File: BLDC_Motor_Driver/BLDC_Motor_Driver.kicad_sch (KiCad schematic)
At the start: 21 parts, among them J1 Conn_01x03_Socket, J2 Conn_01x05_Socket, U1 TMC9660ATB+T, U101 TMC9660, U102 SN74LVC3G17

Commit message: finished power circuitry
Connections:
- net +5V renamed 5V_DRV
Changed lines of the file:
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@@
 	(wire
 		(pts
-			(xy 19.05 111.76) (xy 19.05 114.3)
-		)
-		(stroke
-			(width 0)
-			(type default)
-		)
-	)
-	(wire
-		(pts
 			(xy 34.29 124.46) (xy 36.83 124.46)
 		)
@@
 	(wire
 		(pts
-			(xy 19.05 114.3) (xy 36.83 114.3)
+			(xy 20.32 114.3) (xy 36.83 114.3)
 		)
 		(stroke
@@
 		)
 	)
+	(label "5V_DRV"
+		(at 248.92 121.92 0)
+		(effects
+			(font
+				(size 1.27 1.27)
+			)
+			(justify left bottom)
+		)
+	)
 	(label "DRIVER_CPO"
 		(at -172.72 173.99 0)
@@
 		)
 	)
+	(label "5V_DRV"
+		(at 195.58 107.95 180)
+		(effects
+			(font
+				(size 1.27 1.27)
+			)
+			(justify right bottom)
+		)
+	)
 	(label "HS_Y"
 		(at 175.26 58.42 180)
@@
 		)
 	)
+	(label "5V_DRV"
+		(at 20.32 114.3 180)
+		(effects
+			(font
+				(size 1.27 1.27)
+			)
+			(justify right bottom)
+		)
+	)
 	(label "CSP_V"
 		(at 194.31 39.37 0)
@@
 	)
 	(symbol
-		(lib_id "power:+5V")
-		(at 19.05 111.76 0)
-		(unit 1)
-		(exclude_from_sim no)
-		(in_bom yes)
-		(on_board yes)
-		(dnp no)
-		(property "Reference" "#PWR0120"
-			(at 19.05 115.57 0)
-			(effects
-				(font
-					(size 1.27 1.27)
-				)
-				(hide yes)
-			)
-		)
-		(property "Value" "+5V"
-			(at 19.05 107.95 0)
-			(effects
-				(font
-					(size 1.27 1.27)
-				)
-			)
-		)
-		(property "Footprint" ""
-			(at 19.05 111.76 0)
-			(effects
-				(font
-					(size 1.27 1.27)
-				)
-				(hide yes)
-			)
-		)
-		(property "Datasheet" ""
-			(at 19.05 111.76 0)
-			(effects
-				(font
-					(size 1.27 1.27)
-				)
-				(hide yes)
-			)
-		)
-		(property "Description" "Power symbol creates a global label with name \"+5V\""
-			(at 19.05 111.76 0)
-			(effects
-				(font
-					(size 1.27 1.27)
-				)
-				(hide yes)
-			)
-		)
-		(pin "1"
-		)
-		(instances
-			(project ""
-				(path "/f8816ca8-d12a-4d6e-83e4-586d8ea9408b"
-					(reference "#PWR0120")
-					(unit 1)
-				)
-			)
-		)
-	)
-	(symbol
 		(lib_id "power:GND")
 		(at 46.99 58.42 0)
@@
 	)
 	(symbol
-		(lib_id "power:+5V")
-		(at 195.58 107.95 0)
-		(unit 1)
-		(exclude_from_sim no)
-		(in_bom yes)
-		(on_board yes)
-		(dnp no)
-		(property "Reference" "#PWR0126"
-			(at 195.58 111.76 0)
-			(effects
-				(font
-					(size 1.27 1.27)
-				)
-				(hide yes)
-			)
-		)
-		(property "Value" "+5V"
-			(at 195.58 104.14 0)
-			(effects
-				(font
-					(size 1.27 1.27)
-				)
-			)
-		)
-		(property "Footprint" ""
-			(at 195.58 107.95 0)
-			(effects
-				(font
-					(size 1.27 1.27)
-				)
-				(hide yes)
-			)
-		)
-		(property "Datasheet" ""
-			(at 195.58 107.95 0)
-			(effects
-				(font
-					(size 1.27 1.27)
-				)
-				(hide yes)
-			)
-		)
-		(property "Description" "Power symbol creates a global label with name \"+5V\""
-			(at 195.58 107.95 0)
-			(effects
-				(font
-					(size 1.27 1.27)
-				)
-				(hide yes)
-			)
-		)
-		(pin "1"
-		)
-		(instances
-			(project "BLDC_Motor_Driver"
-				(path "/f8816ca8-d12a-4d6e-83e4-586d8ea9408b"
-					(reference "#PWR0126")
-					(unit 1)
-				)
-			)
-		)
-	)
-	(symbol
 		(lib_id "Device:C")
 		(at 69.85 35.56 0)
@@
 					(unit 1)
 				)
-			)
-		)
-	)
-	(symbol
-		(lib_id "power:+5V")
-		(at 248.92 121.92 0)
-		(unit 1)
-		(exclude_from_sim no)
-		(in_bom yes)
-		(on_board yes)
-		(dnp no)
-		(property "Reference" "#PWR0121"
-			(at 248.92 125.73 0)
-			(effects
-				(font
-					(size 1.27 1.27)
-				)
-				(hide yes)
-			)
-		)
-		(property "Value" "+5V"
-			(at 248.92 118.11 0)
-			(effects
-				(font
-					(size 1.27 1.27)
-				)
-			)
-		)
-		(property "Footprint" ""
-			(at 248.92 121.92 0)
-			(effects
-				(font
-					(size 1.27 1.27)
-				)
-				(hide yes)
-			)
-		)
-		(property "Datasheet" ""
-			(at 248.92 121.92 0)
-			(effects
-				(font
-					(size 1.27 1.27)
-				)
-				(hide yes)
-			)
-		)
-		(property "Description" "Power symbol creates a global label with name \"+5V\""
-			(at 248.92 121.92 0)
-			(effects
-				(font
-					(size 1.27 1.27)
-				)
-				(hide yes)
-			)
-		)
-		(pin "1"
-		)
-		(instances
-			(project "BLDC_Motor_Driver"
-				(path "/f8816ca8-d12a-4d6e-83e4-586d8ea9408b"
-					(reference "#PWR0121")
-					(unit 1)
-				)

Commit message: hall effect done, adding testpoints/connectors
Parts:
- removed U1: TMC9660ATB+T, 21-100060_T6499+2C_ADI, symbol TMC9660ATB:TMC9660ATB+T
- added C112, C114, C115: 1nF, Capacitor_SMD:C_0603_1608Metric, symbol Device:C
- added R111, R112, R113: 4.7k, Resistor_SMD:R_0603_1608Metric, symbol Device:R_US
- added TP101, TP102, TP103, TP104, TP105, TP106, TP107: TestPoint, symbol Connector:TestPoint
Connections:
- net +1V8: now also TP101.1
- net 5V_DRV: now also R111.1, R112.1, R113.1, TP106.1
- net DRIVER_DRV_EN: now also TP104.1
- net DRIVER_FAULTN: now also TP103.1
- net DRIVER_RSTN: now also TP105.1
- net DRIVER_V_{BUCK}: now also TP102.1
- net DRIVER_V_{EXT2}: now also TP107.1
- net GND: now also C112.2, C114.2, C115.2
- net HALL_U_CONN: now also R101.1
- net HALL_V_CONN: now also R102.1
- net HALL_W_CONN: now also R106.1
- net at R102.2: now also U102.3 (2A), C114.1, R112.2
- net at R106.2: now also U102.6 (3A), C112.1, R111.2
- net at R101.2: now also U102.1 (1A), C115.1, R113.2
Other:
- note added: "Testpoints"

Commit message: new GateDriver subsheet. reorg connectors to root sheet
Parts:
- removed C107: 1uF, Capacitor_SMD:C_1206_3216Metric, symbol Device:C
- removed C109: 100nF, Capacitor_SMD:C_0805_2012Metric, symbol Device:C
- removed C110: 100nF, Capacitor_SMD:C_0603_1608Metric, symbol Device:C
- removed C112, C114, C115: 1nF, Capacitor_SMD:C_0603_1608Metric, symbol Device:C
- removed C3: 10uF, Capacitor_SMD:C_0603_1608Metric, symbol Device:C
- removed C4, C5: 10uF, Capacitor_SMD:C_0805_2012Metric, symbol Device:C
- removed C6: 1uF, Capacitor_SMD:C_0603_1608Metric, symbol Device:C
- removed C7: C, symbol Device:C
- removed C8: 10uF, symbol Device:C
- removed L1: 27uH, Inductor_SMD:L_APV_ANR6045, symbol Device:L
- removed R101, R102, R106, R111, R112, R113: 4.7k, Resistor_SMD:R_0603_1608Metric, symbol Device:R_US
- removed U101: TMC9660, Package_QFN:QFN-64-1EP_9x9mm_P0.5mm_EP6.3x6.3mm, symbol Driver_Motor_Analog:TMC9660
- removed U102: SN74LVC3G17, Package_SO:VSSOP-8_2.3x2mm_P0.5mm, symbol Buffer_Texas:SN74LVC3G17
- added D1: RED LED, LED_SMD:LED_0603_1608Metric, symbol Device:LED
- added D2: ORANGE LED, LED_SMD:LED_0603_1608Metric, symbol Device:LED
- added D3: GREEN LED, LED_SMD:LED_0603_1608Metric, symbol Device:LED
- added D4: BLUE LED, LED_SMD:LED_0603_1608Metric, symbol Device:LED
- added J3: Conn_01x02, TerminalBlock_Phoenix:TerminalBlock_Phoenix_MKDS-1-2-3.81_1x02_P3.81mm_Horizontal, symbol Connector_Generic:Conn_01x02
- added J4: USB4105-GF-A, Connector_USB:USB_C_Receptacle_GCT_USB4105-xx-A_16P_TopMnt_Horizontal, symbol Connector:USB_C_Receptacle_USB2.0
- added J5, J6, J7: Conn_01x05, Connector_PinHeader_2.54mm:PinHeader_1x05_P2.54mm_Vertical, symbol Connector_Generic:Conn_01x05
- added J8, J9: Conn_01x04, symbol Connector_Generic:Conn_01x04
- added R11: 10k, Resistor_SMD:R_0603_1608Metric, symbol Device:R_US
- added R12, R13: 5.1k, Resistor_SMD:R_0603_1608Metric, symbol Device:R_US
- added R14, R15, R16, R17: 470, Resistor_SMD:R_0603_1608Metric, symbol Device:R_US
- added SW1, SW2: SW_Push, Button_Switch_SMD:SW_SPST_FSMSM, symbol Switch:SW_Push
- added TP108, TP109, TP110, TP111: ~, symbol Connector:TestPoint
- added U3: ECMF02-2AMX6, Package_DFN_QFN:ST_UQFN-6L_1.5x1.7mm_P0.5mm, symbol Power_Protection:ECMF02-2AMX6
- C1: value 22uF -> 100nF; footprint Capacitor_SMD:C_0805_2012Metric -> Capacitor_SMD:C_0603_1608Metric
- C2: value 10uF -> 100nF
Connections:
- net +36V: now also J3.1 (Pin_1)
- net 5V_DRV: no longer C2.1, TP106.1
- net DRIVER_V_{BUCK}: no longer C1.1
- net GND: now also D1.1 (K), D2.1 (K), D3.1 (K), D4.1 (K), J3.2 (Pin_2), J4.A1 (GND), J4.A12 (GND), J4.B1 (GND), J4.B12 (GND), J4.S1 (SHIELD), J5.5 (Pin_5), J6.5 (Pin_5), J7.5 (Pin_5), J8.4 (Pin_4), J9.4 (Pin_4), R11.2, R12.2, R13.2, SW1.2, TP111.1, U3.3 (GND); no longer C2.2
- new net: D2.2 (A), R15.2
- new net: D3.2 (A), R16.2
- new net: D1.2 (A), R14.2
- new net: D4.2 (A), R17.2
- new net: J4.B5 (CC2), R13.1
- new net: J4.A5 (CC1), R12.1
- new net +3.3V: C2.2, J5.1 (Pin_1), J6.1 (Pin_1), J7.1 (Pin_1), J8.1 (Pin_1), J9.1 (Pin_1), SW2.2, TP108.1
- new net 5V_COM: TP109.1
- new net 5V_REG: TP110.1
- new net BOOT0: C2.1, R11.1, SW2.1
- new net D+: J4.A6 (D+), J4.B6 (D+), U3.6 (D+_out)
- new net D-: J4.A7 (D-), J4.B7 (D-), U3.5 (D-_out)
- new net DRIVER_V_{EXT1}: TP106.1
- new net I2C1_SCL: J8.3 (Pin_3)
- new net I2C1_SDA: J8.2 (Pin_2)
- new net I2C2_SCL: J9.3 (Pin_3)
- new net I2C2_SDA: J9.2 (Pin_2)
- new net LED_BLUE: R17.1
- new net LED_GREEN: R16.1
- new net LED_ORANGE: R15.1
- new net LED_RED: R14.1
- new net NRST: C1.1, J5.4 (Pin_4), SW1.1
- new net SPI1_MISO: J6.3 (Pin_3)
- new net SPI1_MOSI: J6.4 (Pin_4)
- new net SPI1_SCLK: J6.2 (Pin_2)
- new net SPI2_MISO: J7.3 (Pin_3)
- new net SPI2_MOSI: J7.4 (Pin_4)
- new net SPI2_SCLK: J7.2 (Pin_2)
- new net SWCLK: J5.3 (Pin_3)
- new net SWDIO: J5.2 (Pin_2)
- new net USB_D+: U3.1 (D+_in)
- new net USB_D-: U3.2 (D-_in)
- new net USB_POWER: J4.A4 (VBUS), J4.A9 (VBUS), J4.B4 (VBUS), J4.B9 (VBUS)
- no-connect marks 0 -> 4
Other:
- removed sheet H-Bridge-U
- removed sheet H-Bridge-V
- removed sheet H-Bridge-W
- removed sheet H-Bridge-Y
- added sheet Gate-Driver (gate_driver.kicad_sch)
- sheet Microcontroller ports: added 3.3V_REG, BOOT0, I2C1_SCL, I2C1_SDA, I2C2_SCL, I2C2_SDA, LED_BLUE, LED_GREEN, LED_ORANGE, LED_RED, NRST, SPI1_MISO, SPI1_MOSI, SPI1_SCK, SPI2_MISO, SPI2_MOSI, SPI2_SCK, SWCLK, SWDIO, USART1_RX, USART1_TX, USB_D+, USB_D-; removed none
- sheet Power ports: added 3.3V_REG, 36V_VIN, 5V_COM, 5V_REG, USB_POWER; removed none
- note added: "AWG 20, MAX CURR <2A"
- note added: "Connectivity"
- note added: "Debug LEDs"
- note added: "Microcontroller"
- note added: "Power"
- note added: "Power/Serial"
- note added: "Programming"
- note added: "Smart Gate Driver"
- note added: "TODO: add breakout for UART. single channel across external port, uC, and gate driver?"
- note added: "TODO: confirm that UART/SPI channels are necessary for normal operation"
- note added: "TODO: map COMM channel(s) from uC to Gate Driver"
- note added: "TODO: map uC pins to root"
- note added: "TODO: would prefer to have USB conn on top level. open to discussion"
- note added: "USB-C Port"
- note added: "add others"
- note removed: "AWG 20, MAX CURR <2A (TODO: confirm thresholds)"
- note removed: "CSP --> Current Sense Positive CSN --> Current Sense Negative"
- note removed: "H-Bridges"
- note removed: "Hall Effect Sensor"
- note removed: "Motor Driver Passives & Decoupling"
- note removed: "TODO: do we need 4th Y phase? this HBRIDGE interface Y is meant for electric brakes... maybe pursue?"
- note removed: "V_{CC_IO}"
- note removed: "V_{SA}"
- note removed: "V_{S}"
- moved on the sheet: C113, J1, J2, TP101, TP102, TP103, TP104, TP105, TP106, TP107

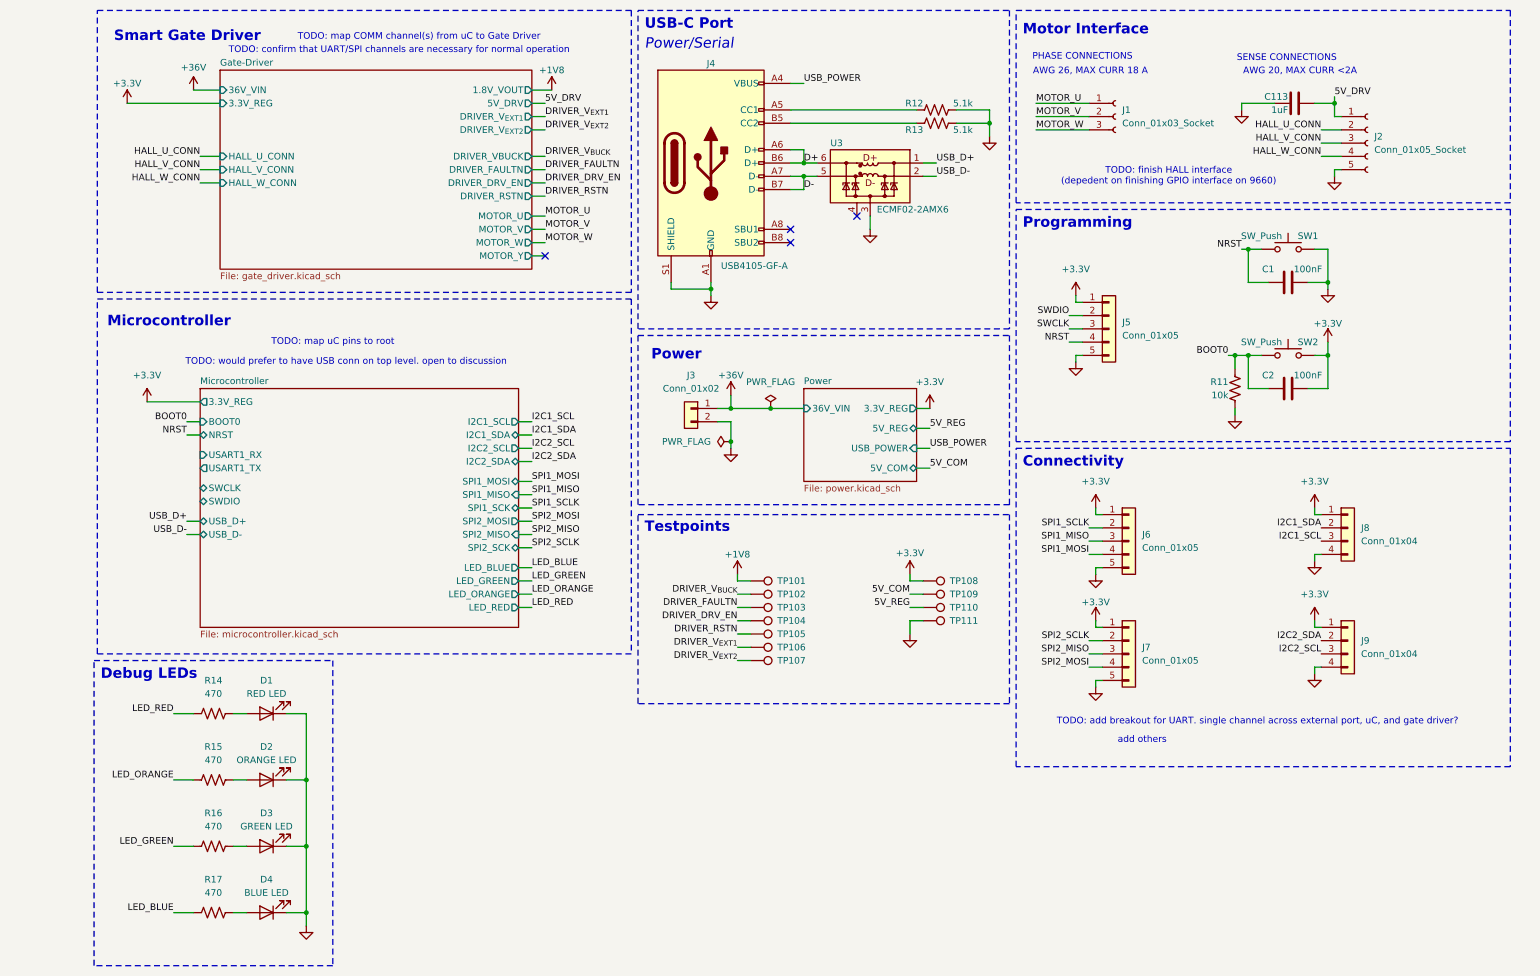
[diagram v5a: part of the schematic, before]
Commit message: added breakout connector and reformatted some things
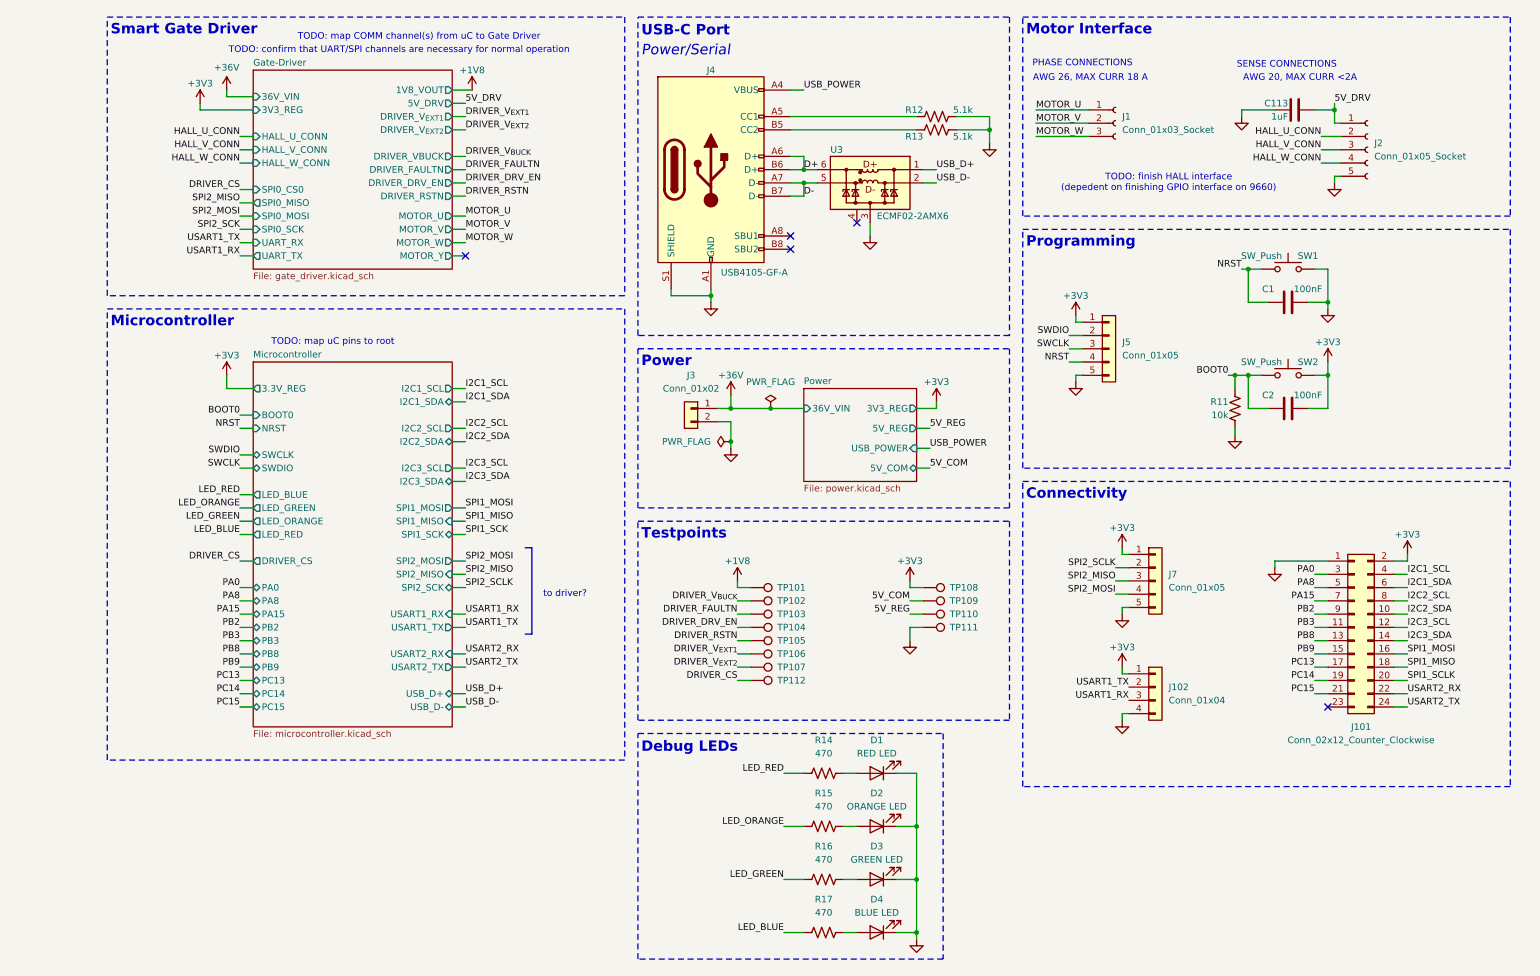
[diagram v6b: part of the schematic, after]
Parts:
- removed J6: Conn_01x05, Connector_PinHeader_2.54mm:PinHeader_1x05_P2.54mm_Vertical, symbol Connector_Generic:Conn_01x05
- removed J8, J9: Conn_01x04, symbol Connector_Generic:Conn_01x04
- added J101: Conn_02x12_Counter_Clockwise, Connector_PinHeader_2.54mm:PinHeader_2x12_P2.54mm_Vertical, symbol Connector_Generic:Conn_02x12_Odd_Even
- added J102: Conn_01x04, symbol Connector_Generic:Conn_01x04
- added TP112: TestPoint, symbol Connector:TestPoint
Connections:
- net GND: now also J101.1 (Pin_1), J102.4 (Pin_4)
- net I2C1_SCL: now also J101.4 (Pin_4)
- net I2C1_SDA: now also J101.6 (Pin_6)
- net I2C2_SCL: now also J101.8 (Pin_8)
- net I2C2_SDA: now also J101.10 (Pin_10)
- net SPI1_MISO: now also J101.18 (Pin_18)
- net SPI1_MOSI: now also J101.16 (Pin_16)
- net SPI1_SCLK: now also J101.20 (Pin_20)
- net +3.3V renamed +3V3
- net +3V3: now also J101.2 (Pin_2), J102.1 (Pin_1)
- new net DRIVER_CS: TP112.1
- new net I2C3_SCL: J101.12 (Pin_12)
- new net I2C3_SDA: J101.14 (Pin_14)
- new net PA0: J101.3 (Pin_3)
- new net PA15: J101.7 (Pin_7)
- new net PA8: J101.5 (Pin_5)
- new net PB2: J101.9 (Pin_9)
- new net PB3: J101.11 (Pin_11)
- new net PB8: J101.13 (Pin_13)
- new net PB9: J101.15 (Pin_15)
- new net PC13: J101.17 (Pin_17)
- new net PC14: J101.19 (Pin_19)
- new net PC15: J101.21 (Pin_21)
- new net USART1_RX: J102.3 (Pin_3)
- new net USART1_TX: J102.2 (Pin_2)
- new net USART2_RX: J101.22 (Pin_22)
- new net USART2_TX: J101.24 (Pin_24)
- no-connect marks 4 -> 5
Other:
- sheet Gate-Driver ports: added 1V8_VOUT, 3V3_REG, SPI0_CS0, SPI0_MISO, SPI0_MOSI, SPI0_SCK, UART_RX, UART_TX; removed 1.8V_VOUT, 3.3V_REG
- sheet Microcontroller ports: added DRIVER_CS, I2C3_SCL, I2C3_SDA, PA0, PA15, PA8, PB2, PB3, PB8, PB9, PC13, PC14, PC15, USART2_RX, USART2_TX; removed none
- sheet Power ports: added 3V3_REG; removed 3.3V_REG
- note added: "to driver?"
- note removed: "TODO: add breakout for UART. single channel across external port, uC, and gate driver?"
- note removed: "TODO: would prefer to have USB conn on top level. open to discussion"
- note removed: "add others"
- moved on the sheet: C1, C113, C2, D1, D2, D3, D4, J1, J2, J4, J5, J7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
